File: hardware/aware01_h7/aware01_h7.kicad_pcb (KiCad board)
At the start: 2 copper layers, 12 parts, among them Q1 MMBT3904, Q2 MMBT3904, U1 STM32H7B0ZBTx, U2 IS45S16800F-7TLA2, U3 10k, U4 10k, U5 10k, U6 10k, U7 LM1117MP-3.3, U8 LM4040DBZ-10

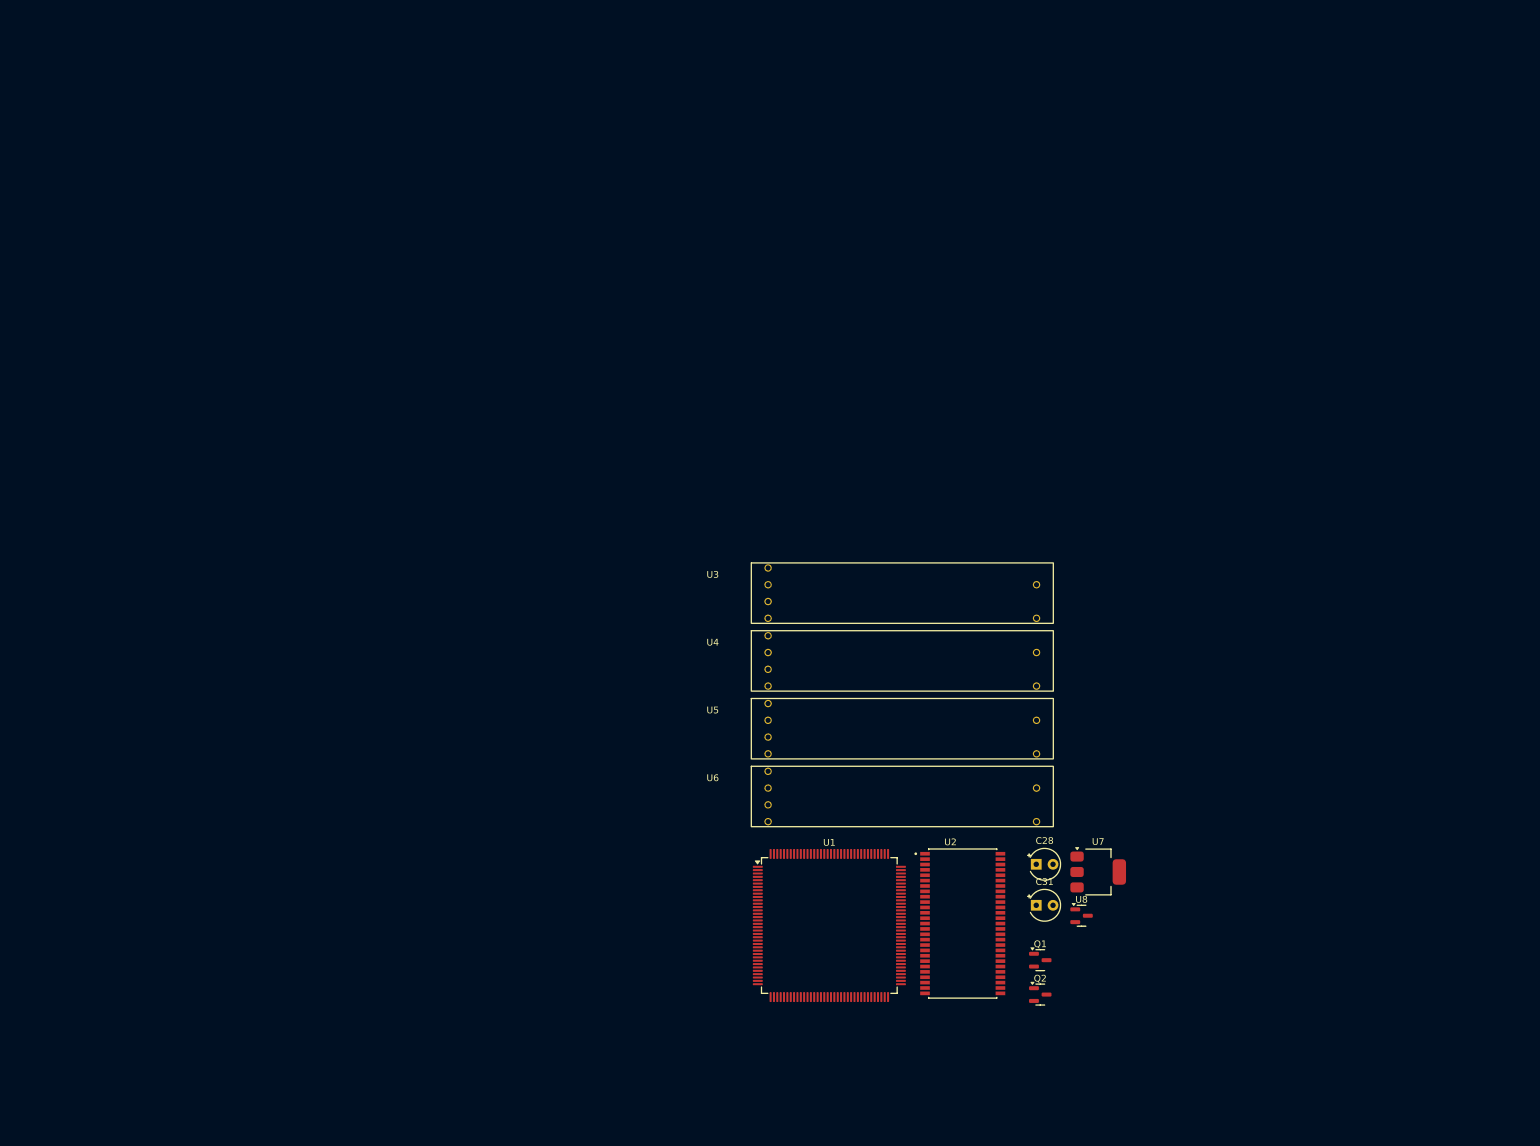
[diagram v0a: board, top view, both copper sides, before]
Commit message: change jack symbols
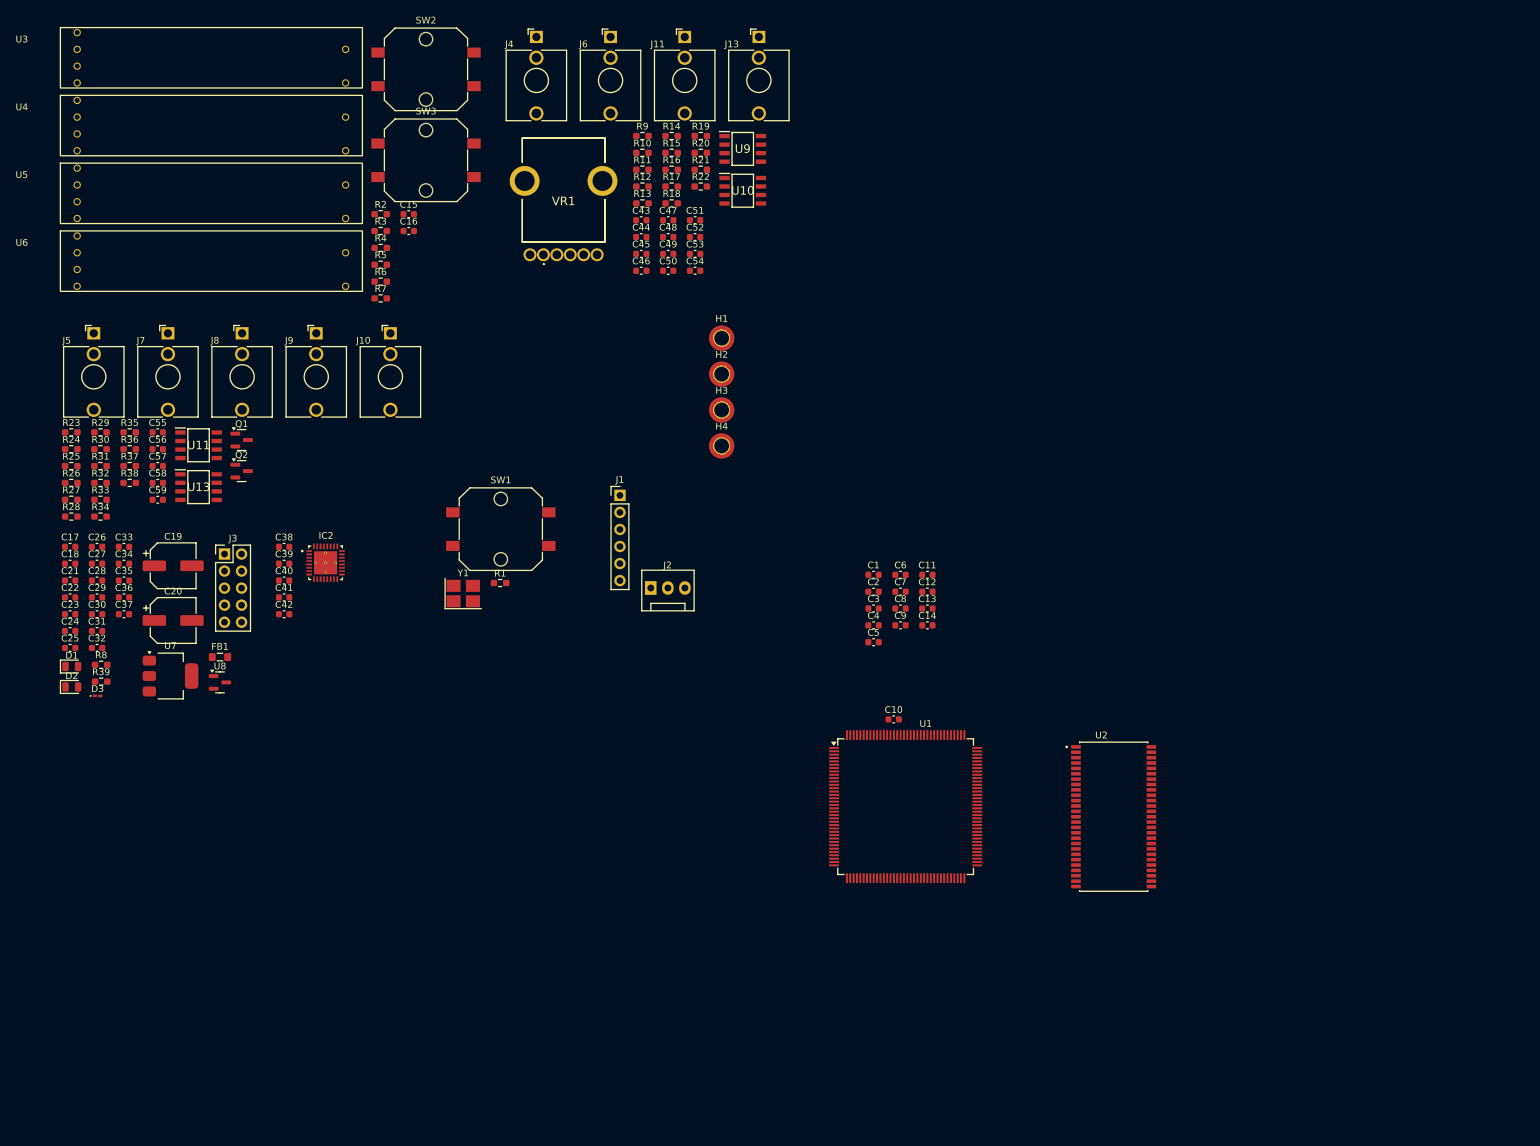
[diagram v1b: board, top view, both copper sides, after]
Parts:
- added C1: 22p, Capacitor_SMD:C_0603_1608Metric, F.Cu at (140.7, 62.5)
- added C10: 100n, Capacitor_SMD:C_0603_1608Metric, F.Cu at (143.7, 84.0)
- added C11: 100n, Capacitor_SMD:C_0603_1608Metric, F.Cu at (148.7, 62.5)
- added C12: 100n, Capacitor_SMD:C_0603_1608Metric, F.Cu at (148.7, 65.0)
- added C13: 100n, Capacitor_SMD:C_0603_1608Metric, F.Cu at (148.7, 67.5)
- added C14: 2.2u, Capacitor_SMD:C_0603_1608Metric, F.Cu at (148.7, 70.0)
- added C15: 100n, Capacitor_SMD:C_0603_1608Metric, F.Cu at (71.5, 8.72)
- added C16: 100n, Capacitor_SMD:C_0603_1608Metric, F.Cu at (71.5, 11.2)
- added C17: 4.7u, Capacitor_SMD:C_0603_1608Metric, F.Cu at (21.0, 58.3)
- added C18: 100n, Capacitor_SMD:C_0603_1608Metric, F.Cu at (21.0, 60.8)
- added C19: 47u, Capacitor_SMD:CP_Elec_6.3x5.9, F.Cu at (36.4, 61.1)
- added C2: 22p, Capacitor_SMD:C_0603_1608Metric, F.Cu at (140.7, 65.0)
- added C20: 47u, Capacitor_SMD:CP_Elec_6.3x5.9, F.Cu at (36.4, 69.3)
- added C21: 100n, Capacitor_SMD:C_0603_1608Metric, F.Cu at (21.0, 63.3)
- added C22: 100n, Capacitor_SMD:C_0603_1608Metric, F.Cu at (21.0, 65.8)
- added C23: 10n, Capacitor_SMD:C_0603_1608Metric, F.Cu at (21.0, 68.3)
- added C24: 100n, Capacitor_SMD:C_0603_1608Metric, F.Cu at (21.0, 70.8)
- added C25: 1u, Capacitor_SMD:C_0603_1608Metric, F.Cu at (21.0, 73.3)
- added C26: 100n, Capacitor_SMD:C_0603_1608Metric, F.Cu at (25.0, 58.3)
- added C27: 100n, Capacitor_SMD:C_0603_1608Metric, F.Cu at (25.0, 60.8)
- added C29: 100n, Capacitor_SMD:C_0603_1608Metric, F.Cu at (25.0, 65.8)
- added C3: 100n, Capacitor_SMD:C_0603_1608Metric, F.Cu at (140.7, 67.5)
- added C30: 10u, Capacitor_SMD:C_0603_1608Metric, F.Cu at (25.0, 68.3)
- added C32: 100n, Capacitor_SMD:C_0603_1608Metric, F.Cu at (25.0, 73.3)
- added C33: 10u, Capacitor_SMD:C_0603_1608Metric, F.Cu at (29.0, 58.3)
- added C34: 100n, Capacitor_SMD:C_0603_1608Metric, F.Cu at (29.0, 60.8)
- added C35: 100n, Capacitor_SMD:C_0603_1608Metric, F.Cu at (29.0, 63.3)
- added C36: 100n, Capacitor_SMD:C_0603_1608Metric, F.Cu at (29.0, 65.8)
- added C37: 100n, Capacitor_SMD:C_0603_1608Metric, F.Cu at (29.0, 68.3)
- added C38: 10u, Capacitor_SMD:C_0603_1608Metric, F.Cu at (52.9, 58.3)
- added C39: 100n, Capacitor_SMD:C_0603_1608Metric, F.Cu at (52.9, 60.8)
- added C4: 100n, Capacitor_SMD:C_0603_1608Metric, F.Cu at (140.7, 70.0)
- added C40: 10u, Capacitor_SMD:C_0603_1608Metric, F.Cu at (52.9, 63.3)
- added C41: 10u, Capacitor_SMD:C_0603_1608Metric, F.Cu at (52.9, 65.8)
- added C42: 100n, Capacitor_SMD:C_0603_1608Metric, F.Cu at (52.9, 68.3)
- added C43: 100n, Capacitor_SMD:C_0603_1608Metric, F.Cu at (106.1, 9.62)
- added C44: 100n, Capacitor_SMD:C_0603_1608Metric, F.Cu at (106.1, 12.1)
- added C45: 1n, Capacitor_SMD:C_0603_1608Metric, F.Cu at (106.1, 14.6)
- added C46: 1n, Capacitor_SMD:C_0603_1608Metric, F.Cu at (106.1, 17.1)
- added C47: 1u, Capacitor_SMD:C_0603_1608Metric, F.Cu at (110.1, 9.62)
- added C48: 1u, Capacitor_SMD:C_0603_1608Metric, F.Cu at (110.1, 12.1)
- added C49: 100n, Capacitor_SMD:C_0603_1608Metric, F.Cu at (110.1, 14.6)
- added C5: 100n, Capacitor_SMD:C_0603_1608Metric, F.Cu at (140.7, 72.5)
- added C50: 100n, Capacitor_SMD:C_0603_1608Metric, F.Cu at (110.1, 17.1)
- added C51: 10u, Capacitor_SMD:C_0603_1608Metric, F.Cu at (114.1, 9.62)
- added C52: 10u, Capacitor_SMD:C_0603_1608Metric, F.Cu at (114.1, 12.1)
- added C53: 220p, Capacitor_SMD:C_0603_1608Metric, F.Cu at (114.1, 14.6)
- added C54: 220p, Capacitor_SMD:C_0603_1608Metric, F.Cu at (114.1, 17.1)
- added C55: 1n, Capacitor_SMD:C_0603_1608Metric, F.Cu at (34.1, 41.2)
- added C56: 1n, Capacitor_SMD:C_0603_1608Metric, F.Cu at (34.1, 43.7)
- added C57: 1n, Capacitor_SMD:C_0603_1608Metric, F.Cu at (34.1, 46.2)
- added C58: 100n, Capacitor_SMD:C_0603_1608Metric, F.Cu at (34.1, 48.8)
- added C59: 100n, Capacitor_SMD:C_0603_1608Metric, F.Cu at (34.1, 51.3)
- added C6: 100n, Capacitor_SMD:C_0603_1608Metric, F.Cu at (144.7, 62.5)
- added C7: 2.2u, Capacitor_SMD:C_0603_1608Metric, F.Cu at (144.7, 65.0)
- added C8: 100n, Capacitor_SMD:C_0603_1608Metric, F.Cu at (144.7, 67.5)
- added C9: 100n, Capacitor_SMD:C_0603_1608Metric, F.Cu at (144.7, 70.0)
- added D1: D, Diode_SMD:D_0805_2012Metric, F.Cu at (21.3, 76.1)
- added D2: D, Diode_SMD:D_0805_2012Metric, F.Cu at (21.3, 79.2)
- added D3: PWR_LED, LED_SMD:LED_0201_0603Metric_Pad0.64x0.40mm_HandSolder, F.Cu at (25.1, 80.5)
- added FB1: 120R, Inductor_SMD:L_0805_2012Metric_Pad1.05x1.20mm_HandSolder, F.Cu at (43.3, 74.7)
- added H1: MountingHole, MountingHole:MountingHole_2.2mm_M2_DIN965_Pad_TopOnly, F.Cu at (118.1, 27.2)
- added H2: MountingHole, MountingHole:MountingHole_2.2mm_M2_DIN965_Pad_TopOnly, F.Cu at (118.1, 32.5)
- added H3: MountingHole, MountingHole:MountingHole_2.2mm_M2_DIN965_Pad_TopOnly, F.Cu at (118.1, 37.9)
- added H4: MountingHole, MountingHole:MountingHole_2.2mm_M2_DIN965_Pad_TopOnly, F.Cu at (118.1, 43.2)
- added IC2: TLV320AIC3204IRHBR, Eurorack:TLV320AIC3204IRHBR, F.Cu at (59.1, 60.7)
- added J1: Conn_01x06_Pin, Connector_PinHeader_2.54mm:PinHeader_1x06_P2.54mm_Vertical, F.Cu at (102.9, 50.6)
- added J10: CV1_IN, Connector_Audio:Jack_3.5mm_QingPu_WQP-PJ398SM_Vertical_CircularHoles, F.Cu at (68.7, 26.5)
- added J11: InL, Connector_Audio:Jack_3.5mm_QingPu_WQP-PJ398SM_Vertical_CircularHoles, F.Cu at (112.6, -17.7)
- added J13: OutR, Connector_Audio:Jack_3.5mm_QingPu_WQP-PJ398SM_Vertical_CircularHoles, F.Cu at (123.6, -17.7)
- added J2: Conn_01x03_Pin, Connector:FanPinHeader_1x03_P2.54mm_Vertical, F.Cu at (107.5, 64.4)
- added J3: Conn_02x05_Odd_Even, Connector_PinHeader_2.54mm:PinHeader_2x05_P2.54mm_Vertical, F.Cu at (44.0, 59.4)
- added J4: InL, Connector_Audio:Jack_3.5mm_QingPu_WQP-PJ398SM_Vertical_CircularHoles, F.Cu at (90.5, -17.7)
- added J5: GATE1_IN, Connector_Audio:Jack_3.5mm_QingPu_WQP-PJ398SM_Vertical_CircularHoles, F.Cu at (24.5, 26.5)
- added J6: OutL, Connector_Audio:Jack_3.5mm_QingPu_WQP-PJ398SM_Vertical_CircularHoles, F.Cu at (101.5, -17.7)
- added J7: GATE2_IN, Connector_Audio:Jack_3.5mm_QingPu_WQP-PJ398SM_Vertical_CircularHoles, F.Cu at (35.6, 26.5)
- added J8: CV2_IN, Connector_Audio:Jack_3.5mm_QingPu_WQP-PJ398SM_Vertical_CircularHoles, F.Cu at (46.6, 26.5)
- added J9: V/OCT_IN, Connector_Audio:Jack_3.5mm_QingPu_WQP-PJ398SM_Vertical_CircularHoles, F.Cu at (57.7, 26.5)
- added R1: 10k, Resistor_SMD:R_0603_1608Metric_Pad0.98x0.95mm_HandSolder, F.Cu at (85.1, 63.7)
- added R10: 22k, Resistor_SMD:R_0603_1608Metric_Pad0.98x0.95mm_HandSolder, F.Cu at (106.3, -0.42)
- added R11: 3.3k, Resistor_SMD:R_0603_1608Metric_Pad0.98x0.95mm_HandSolder, F.Cu at (106.3, 2.09)
- added R12: 3.3k, Resistor_SMD:R_0603_1608Metric_Pad0.98x0.95mm_HandSolder, F.Cu at (106.3, 4.60)
- added R13: 1k, Resistor_SMD:R_0603_1608Metric_Pad0.98x0.95mm_HandSolder, F.Cu at (106.3, 7.11)
- added R14: 1k, Resistor_SMD:R_0603_1608Metric_Pad0.98x0.95mm_HandSolder, F.Cu at (110.6, -2.93)
- added R15: 47k, Resistor_SMD:R_0603_1608Metric_Pad0.98x0.95mm_HandSolder, F.Cu at (110.6, -0.42)
- added R16: 47k, Resistor_SMD:R_0603_1608Metric_Pad0.98x0.95mm_HandSolder, F.Cu at (110.6, 2.09)
- added R17: 3.3k, Resistor_SMD:R_0603_1608Metric_Pad0.98x0.95mm_HandSolder, F.Cu at (110.6, 4.60)
- added R18: 3.3k, Resistor_SMD:R_0603_1608Metric_Pad0.98x0.95mm_HandSolder, F.Cu at (110.6, 7.11)
- added R19: 47k, Resistor_SMD:R_0603_1608Metric_Pad0.98x0.95mm_HandSolder, F.Cu at (115.0, -2.93)
- added R2: 10k, Resistor_SMD:R_0603_1608Metric_Pad0.98x0.95mm_HandSolder, F.Cu at (67.3, 8.72)
- added R20: 47k, Resistor_SMD:R_0603_1608Metric_Pad0.98x0.95mm_HandSolder, F.Cu at (115.0, -0.42)
- added R21: 1k, Resistor_SMD:R_0603_1608Metric_Pad0.98x0.95mm_HandSolder, F.Cu at (115.0, 2.09)
- added R22: 1k, Resistor_SMD:R_0603_1608Metric_Pad0.98x0.95mm_HandSolder, F.Cu at (115.0, 4.60)
- added R23: 100k, Resistor_SMD:R_0603_1608Metric_Pad0.98x0.95mm_HandSolder, F.Cu at (21.2, 41.2)
- added R24: 100k, Resistor_SMD:R_0603_1608Metric_Pad0.98x0.95mm_HandSolder, F.Cu at (21.2, 43.7)
- added R25: 200k, Resistor_SMD:R_0603_1608Metric_Pad0.98x0.95mm_HandSolder, F.Cu at (21.2, 46.2)
- added R26: 100k, Resistor_SMD:R_0603_1608Metric_Pad0.98x0.95mm_HandSolder, F.Cu at (21.2, 48.8)
- added R27: 10k, Resistor_SMD:R_0603_1608Metric_Pad0.98x0.95mm_HandSolder, F.Cu at (21.2, 51.3)
- added R28: 10k, Resistor_SMD:R_0603_1608Metric_Pad0.98x0.95mm_HandSolder, F.Cu at (21.2, 53.8)
- added R29: 33k, Resistor_SMD:R_0603_1608Metric_Pad0.98x0.95mm_HandSolder, F.Cu at (25.5, 41.2)
- added R3: 10k, Resistor_SMD:R_0603_1608Metric_Pad0.98x0.95mm_HandSolder, F.Cu at (67.3, 11.2)
- added R30: 100k, Resistor_SMD:R_0603_1608Metric_Pad0.98x0.95mm_HandSolder, F.Cu at (25.5, 43.7)
- added R31: 180k, Resistor_SMD:R_0603_1608Metric_Pad0.98x0.95mm_HandSolder, F.Cu at (25.5, 46.2)
- added R32: 100k, Resistor_SMD:R_0603_1608Metric_Pad0.98x0.95mm_HandSolder, F.Cu at (25.5, 48.8)
- added R33: 200k, Resistor_SMD:R_0603_1608Metric_Pad0.98x0.95mm_HandSolder, F.Cu at (25.5, 51.3)
- added R34: 100k, Resistor_SMD:R_0603_1608Metric_Pad0.98x0.95mm_HandSolder, F.Cu at (25.5, 53.8)
- added R35: 47k, Resistor_SMD:R_0603_1608Metric_Pad0.98x0.95mm_HandSolder, F.Cu at (29.9, 41.2)
- added R36: 33k, Resistor_SMD:R_0603_1608Metric_Pad0.98x0.95mm_HandSolder, F.Cu at (29.9, 43.7)
- added R37: 100k, Resistor_SMD:R_0603_1608Metric_Pad0.98x0.95mm_HandSolder, F.Cu at (29.9, 46.2)
- added R38: 100k, Resistor_SMD:R_0603_1608Metric_Pad0.98x0.95mm_HandSolder, F.Cu at (29.9, 48.8)
- added R39: 150, Resistor_SMD:R_0603_1608Metric_Pad0.98x0.95mm_HandSolder, F.Cu at (25.6, 78.4)
- added R4: 75, Resistor_SMD:R_0603_1608Metric_Pad0.98x0.95mm_HandSolder, F.Cu at (67.3, 13.7)
- added R5: 75, Resistor_SMD:R_0603_1608Metric_Pad0.98x0.95mm_HandSolder, F.Cu at (67.3, 16.2)
- added R6: 75, Resistor_SMD:R_0603_1608Metric_Pad0.98x0.95mm_HandSolder, F.Cu at (67.3, 18.8)
- added R7: 75, Resistor_SMD:R_0603_1608Metric_Pad0.98x0.95mm_HandSolder, F.Cu at (67.3, 21.3)
- added R8: 470, Resistor_SMD:R_0603_1608Metric_Pad0.98x0.95mm_HandSolder, F.Cu at (25.6, 75.9)
- added R9: 22k, Resistor_SMD:R_0603_1608Metric_Pad0.98x0.95mm_HandSolder, F.Cu at (106.3, -2.93)
- added SW1: SW_Push, Button_Switch_SMD:SW_Push_1P1T_NO_CK_PTS125Sx43PSMTR, F.Cu at (85.2, 55.6)
- added SW2: SW_Push, Button_Switch_SMD:SW_Push_1P1T_NO_CK_PTS125Sx43PSMTR, F.Cu at (74.0, -12.9)
- added SW3: SW_Push, Button_Switch_SMD:SW_Push_1P1T_NO_CK_PTS125Sx43PSMTR, F.Cu at (74.0, 0.69)
- added U10: NE5532DRG4, Eurorack:NE5532DRG4, F.Cu at (121.2, 5.23)
- added U11: LMV722IDR, Eurorack:LMV722IDR, F.Cu at (40.1, 43.2)
- added U13: LMV722IDR, Eurorack:LMV722IDR, F.Cu at (40.1, 49.4)
- added U9: NE5532DRG4, Eurorack:NE5532DRG4, F.Cu at (121.2, -1.00)
- added VR1: PTV112-4420A-B503, Eurorack:PTV1124420AB503, F.Cu at (91.5, 14.8)
- added Y1: WE-XTAL 24.0MHz 50ppm, Crystal:Crystal_SMD_3225-4Pin_3.2x2.5mm_HandSoldering, F.Cu at (79.6, 65.2)
- C28: value 10u -> 1u; footprint Capacitor_THT:CP_Radial_Tantal_D4.5mm_P2.50mm -> Capacitor_SMD:C_0603_1608Metric
- C31: value 10u -> 100n; footprint Capacitor_THT:CP_Radial_Tantal_D4.5mm_P2.50mm -> Capacitor_SMD:C_0603_1608Metric
- U2: footprint Eurorack:SOP80P1176X120-54N -> Eurorack:IS45S16800F-7TLA2
- moved C28 146.2 mm to (25.0, 63.3)
- moved C31 145.8 mm to (25.0, 70.8)
- moved Q2 142.3 mm to (46.6, 47.0)
- moved Q1 142.0 mm to (46.6, 42.4)
- moved U7 141.3 mm to (36.0, 77.5)
- moved U8 133.0 mm to (43.3, 78.5)
- moved U3 130.2 mm to (22.1, -14.6)
- moved U4 130.2 mm to (22.1, -4.49)
- moved U5 130.2 mm to (22.1, 5.62)
- moved U6 130.2 mm to (22.1, 15.7)
- moved U2 27.6 mm to (176.5, 98.5)
- moved U1 21.0 mm to (145.5, 97.0)
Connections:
- C28 pad 1: +12V -> +3.3V
- U1 pad 133: unconnected-(U1-PB3-Pad133) -> /SWO
- U1 pad 95: unconnected-(U1-VDD33_USB-Pad95) -> +3.3V
- U3 pad 1: +3V3 -> +3.3V
- U4 pad 1: +3V3 -> +3.3V
- U5 pad 1: +3V3 -> +3.3V
- U6 pad 1: +3V3 -> +3.3V

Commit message: update pcb
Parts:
- removed H1, H2, H3, H4: MountingHole, MountingHole:MountingHole_2.2mm_M2_DIN965_Pad_TopOnly
- added C60: 100n, Capacitor_SMD:C_0603_1608Metric, B.Cu at (230.8, 95.2)
- added C61: 100n, Capacitor_SMD:C_0603_1608Metric, B.Cu at (180.6, 64.8)
- added C62: 100n, Capacitor_SMD:C_0603_1608Metric, B.Cu at (204.7, 60.0)
- added C63: 100n, Capacitor_SMD:C_0603_1608Metric, B.Cu at (181.2, 80.2)
- C1, C10, C11, C12, C13, C14, C17, C18, C19, C2, C20, C21, C22, C23, C24, C25, C26, C27, C28, C29, C3, C30, C31, C32, C33, C34, C35, C36, C37, C38, C39, C4, C40, C41, C42, C43, C44, C45, C46, C47, C48, C49, C5, C50, C51, C52, C53, C54, C55, C56, C57, C58, C59, C6, C7, C8, C9, D1, D2, FB1, IC2, J1, Q1, Q2, R1, R10, R11, R12, R13, R14, R15, R16, R17, R18, R19, R20, R21, R22, R23, R24, R25, R26, R27, R28, R29, R30, R31, R32, R33, R34, R35, R36, R37, R38, R39, R4, R5, R6, R7, R8, R9, U1, U10, U11, U13, U2, U7, U8, U9, Y1: moved to B.Cu
- D3: footprint LED_SMD:LED_0201_0603Metric_Pad0.64x0.40mm_HandSolder -> LED_SMD:LED_0603_1608Metric_Pad1.05x0.95mm_HandSolder; moved to B.Cu
- J10, J11, J13, J5, J6, J7, J8, J9: footprint Connector_Audio:Jack_3.5mm_QingPu_WQP-PJ398SM_Vertical_CircularHoles -> Eurorack:THONK_PJ398SM-12
- J2: footprint Connector:FanPinHeader_1x03_P2.54mm_Vertical -> Connector_PinHeader_2.54mm:PinHeader_1x03_P2.54mm_Vertical; moved to B.Cu
- J3: footprint Connector_PinHeader_2.54mm:PinHeader_2x05_P2.54mm_Vertical -> Eurorack:PinHeader_2x05_P2.54mm_BHR-10-VUA; moved to B.Cu
- J4: value InL -> InR; footprint Connector_Audio:Jack_3.5mm_QingPu_WQP-PJ398SM_Vertical_CircularHoles -> Eurorack:THONK_PJ398SM-12
- SW1: footprint Button_Switch_SMD:SW_Push_1P1T_NO_CK_PTS125Sx43PSMTR -> Eurorack:TS046643BK100SMT; moved to B.Cu
- SW2, SW3: footprint Button_Switch_SMD:SW_Push_1P1T_NO_CK_PTS125Sx43PSMTR -> Button_Switch_THT:SW_PUSH_6mm_H13mm
- U3, U4, U5, U6: footprint Bourns Fader:PTL30-15R1-103B2 -> Eurorack:PTL30-15R1-103B2
- moved R26 229.6 mm to (233.2, 136.8), turned to 90 degrees
- moved R29 224.9 mm to (233.2, 127.5)
- moved R30 224.6 mm to (235.0, 124.8), turned to -90 degrees
- moved U6 219.8 mm to (227.8, 93.0), turned to 90 degrees
- moved R25 217.6 mm to (226.8, 117.8), turned to -90 degrees
- moved C55 214.6 mm to (231.8, 124.8), turned to 90 degrees
- moved J8 214.2 mm to (230.5, 136.4), turned to 180 degrees
- moved R34 213.3 mm to (222.0, 136.8), turned to 90 degrees
- moved C25 211.9 mm to (232.2, 90.5)
- moved C23 209.6 mm to (229.5, 89.5), turned to 90 degrees
- moved C28 208.4 mm to (232.2, 85.0)
- moved R32 205.3 mm to (211.0, 136.8), turned to 90 degrees
- moved U5 205.2 mm to (207.8, 93.0), turned to 90 degrees
- moved U11 203.5 mm to (226.0, 126.0), turned to 180 degrees
- moved R33 201.7 mm to (216.0, 117.8), turned to -90 degrees
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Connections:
- D3 pad 1: GND -> Net-(D3-K)
- D3 pad 2: Net-(D3-A) -> +3.3V
- R39 pad 1: +3.3V -> Net-(D3-K)
- R39 pad 2: Net-(D3-A) -> GND
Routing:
- net GND: track 0.00 -> 202.8 mm, vias 0 -> 93
- net /V_OCT_IN: track 0.00 -> 128.2 mm, vias 0 -> 4
- net -12V: track 0.00 -> 121.6 mm, vias 0 -> 2
- net +3.3V: track 0.00 -> 113.7 mm, vias 0 -> 36
- net +3.3VA: track 0.00 -> 113.3 mm, vias 0 -> 3
- net /CV2_IN: track 0.00 -> 109.2 mm, vias 0 -> 6
- net +12V: track 0.00 -> 108.8 mm, vias 0 -> 4
- net /NRST: track 0.00 -> 106.1 mm, vias 0 -> 2
- net /I2S1_WS: track 0.00 -> 96.3 mm
- net /I2S1_CK: track 0.00 -> 92.8 mm
- net /I2S1_MCK: track 0.00 -> 88.8 mm
- net /CV1_IN: track 0.00 -> 88.2 mm, vias 0 -> 4
- net /GATE1_IN: track 0.00 -> 76.8 mm, vias 0 -> 2
- net /GATE2_IN: track 0.00 -> 72.8 mm
- net /SWDIO: track 0.00 -> 72.7 mm, vias 0 -> 3
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- added copper zone on B.Cu, net +12V
- added copper zone on B.Cu, net +3.3V
- added copper zone on In1.Cu, net +3.3V
- added copper zone on B.Cu, net GND
- added copper zone on In2.Cu, net GND
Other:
- board outline added: 76.2 x 110 mm
- copper layers 2 -> 4

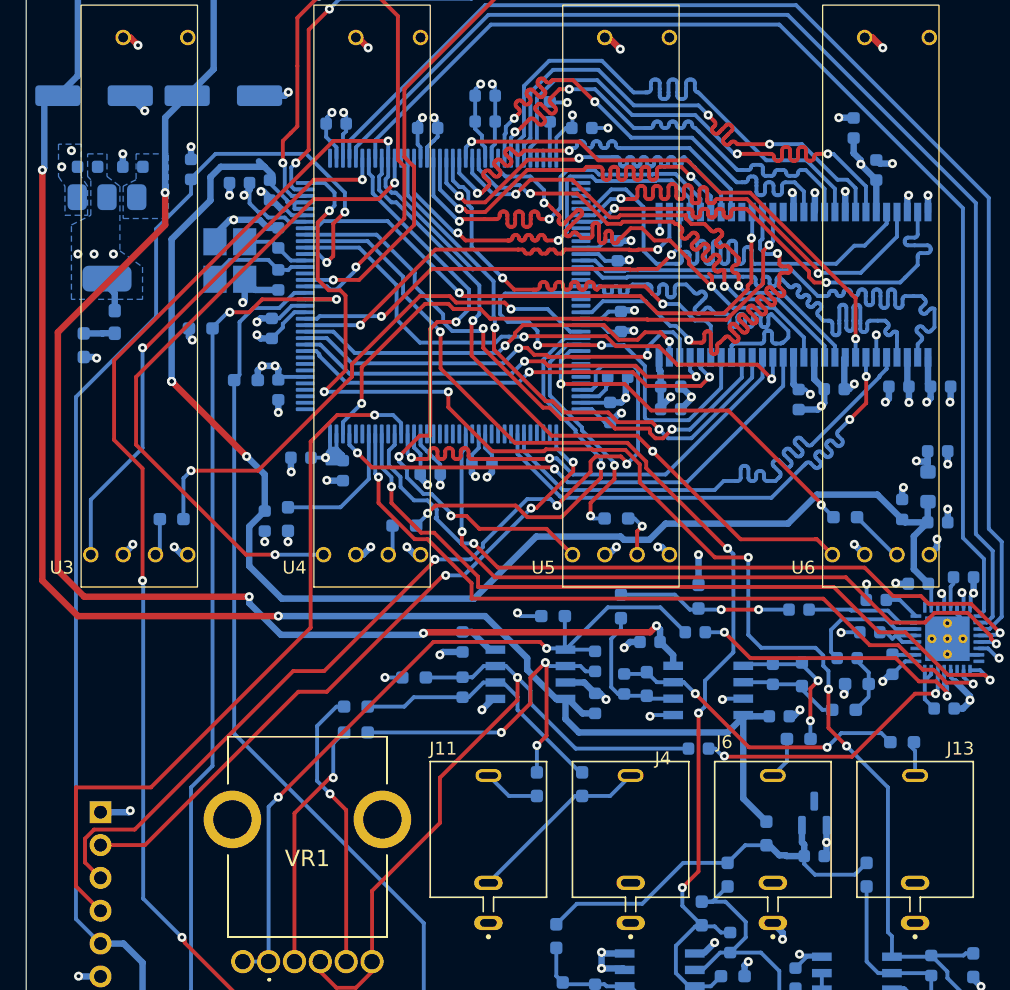
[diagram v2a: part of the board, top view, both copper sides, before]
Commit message: minor layout adjustments
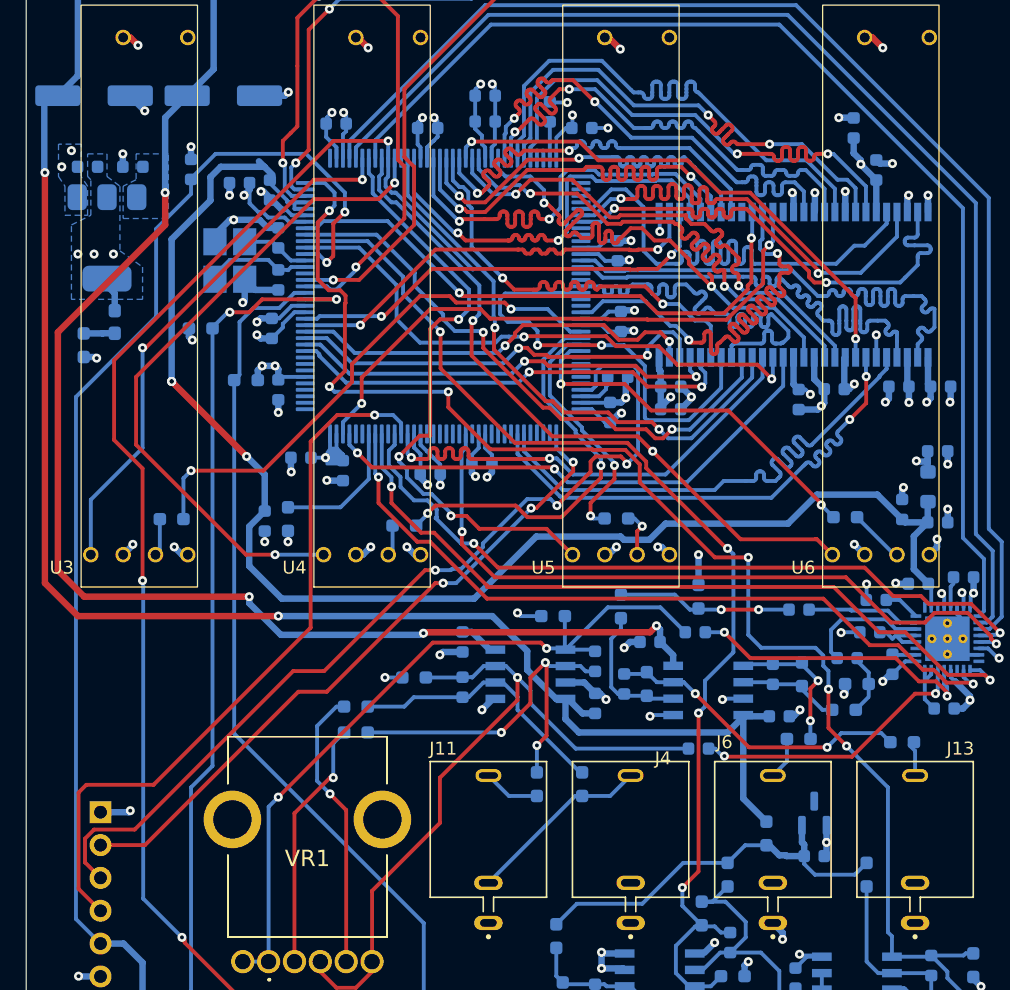
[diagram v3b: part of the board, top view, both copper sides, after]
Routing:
- net /FMC_D2: track 44.1 -> 42.9 mm
- net /FMC_D3: track 40.7 -> 39.7 mm
- net /FMC_D0: track 43.7 -> 42.7 mm
- net /CV2_IN: track 109.2 -> 108.3 mm
- net /FMC_NBL1: track 46.6 -> 45.8 mm
- net /I2C1_SDA: track 59.4 -> 58.7 mm
- net /FMC_D1: track 43.2 -> 42.6 mm
- net /FMC_SDNE0: track 46.0 -> 45.3 mm
- net /SWO: track 56.9 -> 56.4 mm
